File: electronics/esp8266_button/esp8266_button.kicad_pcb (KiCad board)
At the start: 2 copper layers, 34.3 x 50.8 mm, 30 parts, among them J1 CONN_01X03, J2 CONN_01X08, J3 CONN_01X08, M1 BMP180_Breakout, P1 SYMBOL, Q1 Q_NMOS_GSD, Q2 Q_PMOS_GSD, SW1 SW_Push, SW2 SW_Push, SW3 SW_Push, U1 MCP1703A-3302/MB, U2 ESP-12

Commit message: Begin next button version
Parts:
- P1: value SYMBOL -> OSHW
- R7: value R -> 320k
- R8: value R -> 100k
- U2: footprint ESP8266:ESP-12 -> ESP8266:ESP-12E
- moved U2 9.88 mm to (154.3, 94.0)
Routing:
- net GPIO0: track 31.0 -> 35.2 mm
- net GND: track 29.1 -> 31.8 mm, vias 5 -> 6
- net CH_PD: track 32.6 -> 34.7 mm
- net RESET: track 28.2 -> 30.0 mm, vias 1 -> 3
- net /GPIO5: track 16.2 -> 16.9 mm
- net /GPIO4: track 17.5 -> 18.1 mm
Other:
- board text added: "esp8266_button v1.?"
- board text added: "github.com/google/makerspace-partsbin electronics/esp8266_button"
- board text removed: "Kapton ->"
- board text removed: "esp8266_button v1"

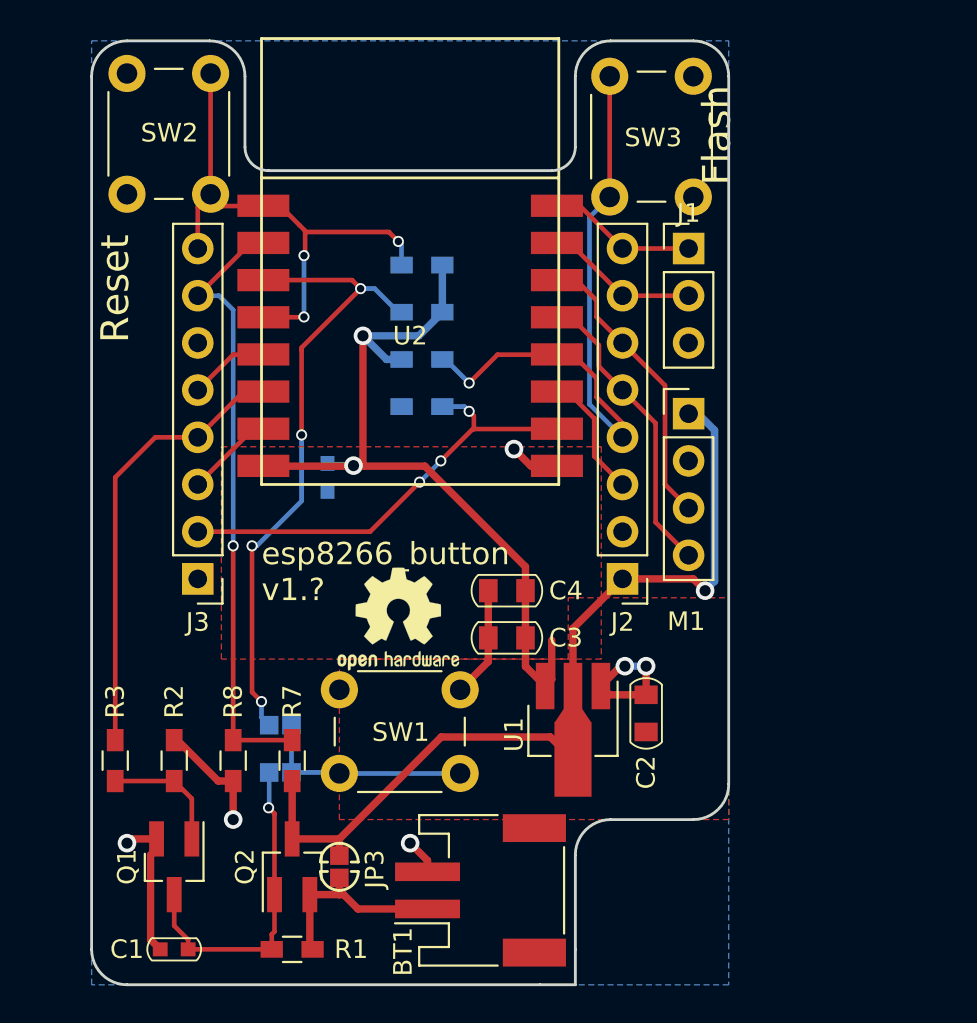
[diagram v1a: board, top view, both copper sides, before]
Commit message: esp_button almost to v1.1
Easier to solder
* Mostly 0805, with some 1206 for larger caps
* Battery connector is your choice of through hole or SMT
* Fiducials, just in case

Easier to program
* Full FTDI connector
* Auto-reset
* Pogo version below
* More obvious/accessible solder jumpers on top

Better performance
* Temperature sensor moved away from regulator :)
* Battery monitor and temperature sensor moved behind mosfet, reducing
  theoretical deep-sleep current by about 16uA

Easier to make a case for
* (Mostly) metric grid, larger board (40x50mm)
* Mounting holes (32x42mm)
* Big button slightly more centered
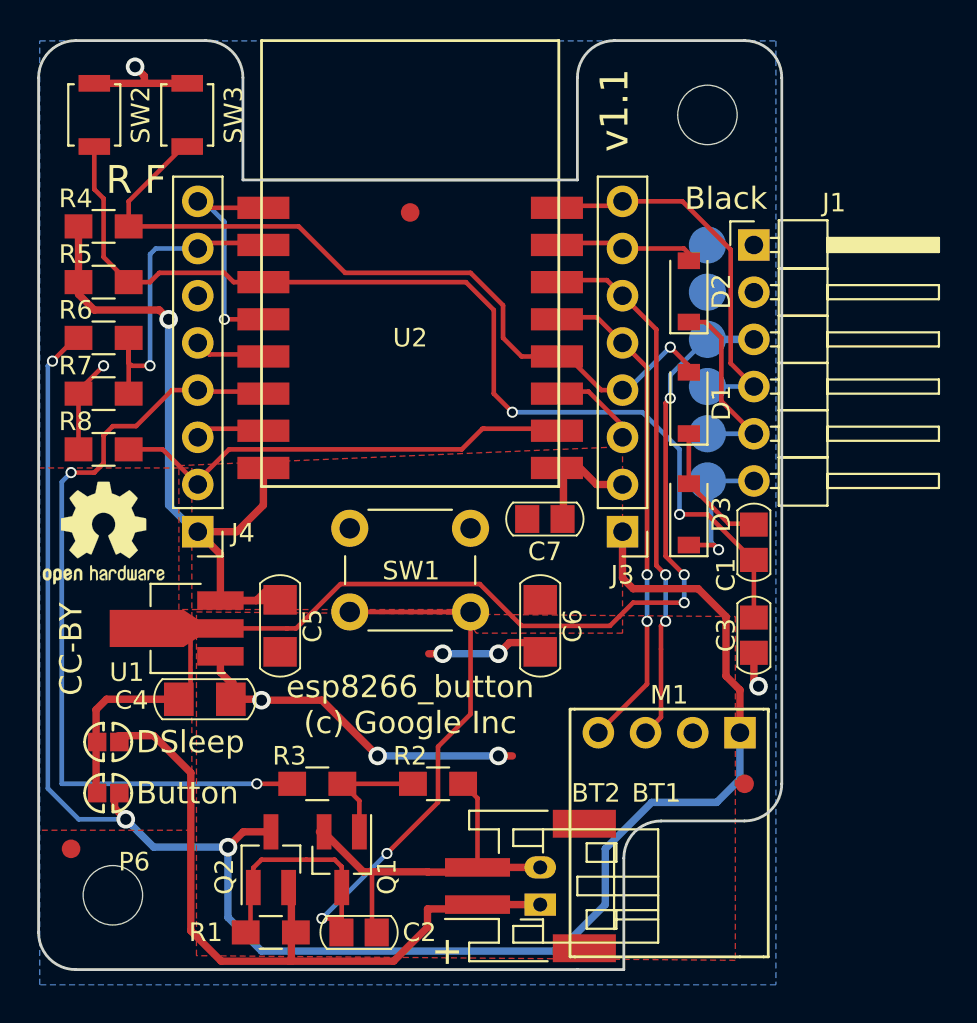
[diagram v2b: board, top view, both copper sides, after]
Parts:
- removed the JP1 at (147.3, 114.9)
- removed R9: 10k, Resistors_SMD:R_0603_HandSoldering
- added BT1: Battery_Cell, Connectors_JST:JST_PH_S2B-PH-K_02x2.00mm_Angled, F.Cu at (161.3, 124.6)
- added C6: 10u, Capacitors_SMD_Round:C_1206, F.Cu at (161.3, 109.6)
- added C7: 220p, Capacitors_SMD_Round:C_0805, F.Cu at (161.6, 103.8)
- added D1: B5819W, Diodes_SMD:D_SOD-123, F.Cu at (169.3, 97.6)
- added D2: B5819W, Diodes_SMD:D_SOD-123, F.Cu at (169.3, 91.6)
- added D3: B5819W, Diodes_SMD:D_SOD-123, F.Cu at (169.3, 103.6)
- added J2: CONN_01X06, Pogo_Pads:Pogo_6, B.Cu at (170.3, 89.1)
- added P2: M3 Hole, Mounting_Holes:MountingHole_3.2mm_M3, F.Cu at (138.3, 124.1)
- added P3: M3 Hole, Mounting_Holes:MountingHole_3.2mm_M3, F.Cu at (170.3, 82.1)
- added P4: Fid, Fiducials:Fiducial_1mm_Dia_2.54mm_Outer_CopperTop, F.Cu at (154.3, 87.3)
- added P5: Fid, Fiducials:Fiducial_1mm_Dia_2.54mm_Outer_CopperTop, F.Cu at (172.3, 118.1)
- added P6: Fid, Fiducials:Fiducial_1mm_Dia_2.54mm_Outer_CopperTop, F.Cu at (136.1, 121.6)
- C1: footprint Capacitors_SMD_Round:C_0603 -> Capacitors_SMD_Round:C_0805
- C2, C3: value 10u -> 220p
- C4: footprint Capacitors_SMD_Round:C_0805 -> Capacitors_SMD_Round:C_1206
- C5: value 0.1u -> 10u; footprint Capacitors_SMD_Round:C_0603 -> Capacitors_SMD_Round:C_1206; moved to F.Cu
- J1: value CONN_01X03 -> CONN_01X06; footprint Pin_Headers:Pin_Header_Straight_1x03_Pitch2.54mm -> Pin_Headers:Pin_Header_Angled_1x06_Pitch2.54mm
- JP2: value Button=PowerOn -> MOS Control; moved to F.Cu
- M1: footprint Pin_Headers:Pin_Header_Straight_1x04_Pitch2.54mm -> Breakout_Modules:BMxx80
- R1, R2, R3: footprint Resistors_SMD:R_0603_HandSoldering -> Resistors_SMD:R_0805_HandSoldering
- R4, R5: footprint Resistors_SMD:R_0603_HandSoldering -> Resistors_SMD:R_0805_HandSoldering; moved to F.Cu
- R6: value 10k -> 320k; footprint Resistors_SMD:R_0603_HandSoldering -> Resistors_SMD:R_0805_HandSoldering; moved to F.Cu
- R7: value 320k -> 100k; footprint Resistors_SMD:R_0603_HandSoldering -> Resistors_SMD:R_0805_HandSoldering
- R8: value 100k -> 10k; footprint Resistors_SMD:R_0603_HandSoldering -> Resistors_SMD:R_0805_HandSoldering
- SW2, SW3: footprint Buttons_Switches_THT:SW_PUSH_6mm -> Buttons_Switches_SMD:SW_SPST_B3U-1000P
- moved C1 38.1 mm to (172.8, 105.1), turned to 270 degrees
- moved SW3 27.3 mm to (142.3, 82.1)
- moved R7 22.2 mm to (137.8, 97.1), turned to 180 degrees
- moved U1 21.6 mm to (142.1, 109.7), turned to 180 degrees
- moved C2 19.4 mm to (151.6, 126.1), turned to 0 degrees
- moved R8 18.1 mm to (137.8, 100.1), turned to 0 degrees
- moved R5 17.6 mm to (137.8, 91.1), turned to 180 degrees
- moved M1 17.4 mm to (172.1, 115.3)
- moved C4 17.3 mm to (143.3, 113.5), turned to 0 degrees
- moved R4 17.3 mm to (137.8, 88.1)
- moved R6 17.2 mm to (137.8, 94.1), turned to 0 degrees
- moved P1 16.5 mm to (137.8, 104.6)
- moved R2 14.3 mm to (155.8, 118.1), turned to 0 degrees
- moved JP1 14.1 mm to (138.1, 115.8), turned to 180 degrees
- moved C3 13.3 mm to (172.8, 110.1), turned to 90 degrees
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- renumbered BT1 to BT2, J2 to J3, J3 to J4, JP3 to JP1
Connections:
- C1 pad 1: ~POWERON -> Net-(C1-Pad1)
- C1 pad 2: GND -> CH_PD
- C2 pad 1: BATTMON -> ~POWERON
- C3 pad 1: +3V3 -> GND
- C3 pad 2: GND -> CH_PD
- C4 pad 1: +3V3 -> PWRIN
- J1 pad 1: /TXD -> GND
- J1 pad 2: /RXD -> (no net)
- J1 pad 3: GND -> PWRIN
- J3 pad 7: /RXD -> RXD
- J3 pad 8: /TXD -> TXD
- J4 pad 1: (no net) -> +3V3
- J4 pad 8: RESET -> /RESET
- JP1 pad 2: BATTMON -> PWRIN
- JP2 pad 1: Net-(JP1-Pad1) -> BATTMON
- JP2 pad 2: ~POWERON -> PWRIN
- R4 pad 1: +3V3 -> GPIO0
- R4 pad 2: RESET -> +3V3
- R5 pad 1: +3V3 -> CH_PD
- R5 pad 2: GPIO0 -> +3V3
- R6 pad 1: +3V3 -> BATTMON
- R6 pad 2: CH_PD -> /ADC
- R7 pad 1: BATTMON -> /ADC
- R7 pad 2: /ADC -> GND
- R8 pad 1: /ADC -> GND
- R8 pad 2: GND -> /GPIO15
- SW1 pad 2: Net-(JP1-Pad1) -> ~POWERON
- SW2 pad 2: RESET -> CH_PD
- U1 pad 2: BATTMON -> PWRIN
- U2 pad 1: RESET -> /RESET
- U2 pad 15: /RXD -> RXD
- U2 pad 16: /TXD -> TXD
- U2 pad 4: RESET -> /RESET
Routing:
- net PWRIN: track 0.00 -> 62.3 mm, vias 0 -> 3
- net BATTMON: track 44.1 -> 96.2 mm, vias 1 -> 3
- net GND: track 31.8 -> 67.4 mm, vias 6 -> 8
- net RESET: track 30.0 -> 0.00 mm, vias 3 -> 0
- net /Vbat: track 10.6 -> 38.9 mm
- net TXD: track 0.00 -> 23.0 mm
- net ~POWERON: track 17.5 -> 39.8 mm, vias 1 -> 2
- net CH_PD: track 34.7 -> 56.1 mm, vias 4 -> 2
- net GPIO12: track 24.9 -> 44.5 mm, vias 0 -> 2
- net /ADC: track 34.3 -> 19.5 mm
- net /GPIO5: track 16.9 -> 30.9 mm, vias 0 -> 2
- net /RESET: track 0.00 -> 13.3 mm, vias 0 -> 1
- net Net-(JP1-Pad1): track 11.6 -> 0.00 mm
- net /GPIO4: track 18.1 -> 29.4 mm, vias 0 -> 2
- net Net-(D2-Pad1): track 0.00 -> 10.3 mm
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- added copper zone on F.Cu, net GND
- added copper zone on F.Cu, net PWRIN
- removed copper zone on F.Cu, net BATTMON
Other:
- board size 34.3 x 50.8 mm -> 40 x 50 mm
- board text added: "+"
- board text added: "Black"
- board text added: "Button"
- board text added: "CC-BY"
- board text added: "DSleep"
- board text added: "GND"
- board text added: "IO2"
- board text added: "R F"
- board text added: "SCL"
- board text added: "SDA"
- board text added: "esp8266_button (c) Google Inc"
- board text added: "v1.1"
- board text removed: "Flash"
- board text removed: "Reset"
- board text removed: "esp8266_button v1.?"
- board text removed: "tx rx gnd"

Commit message: Aesthetic tweaks to esp_button 1.1
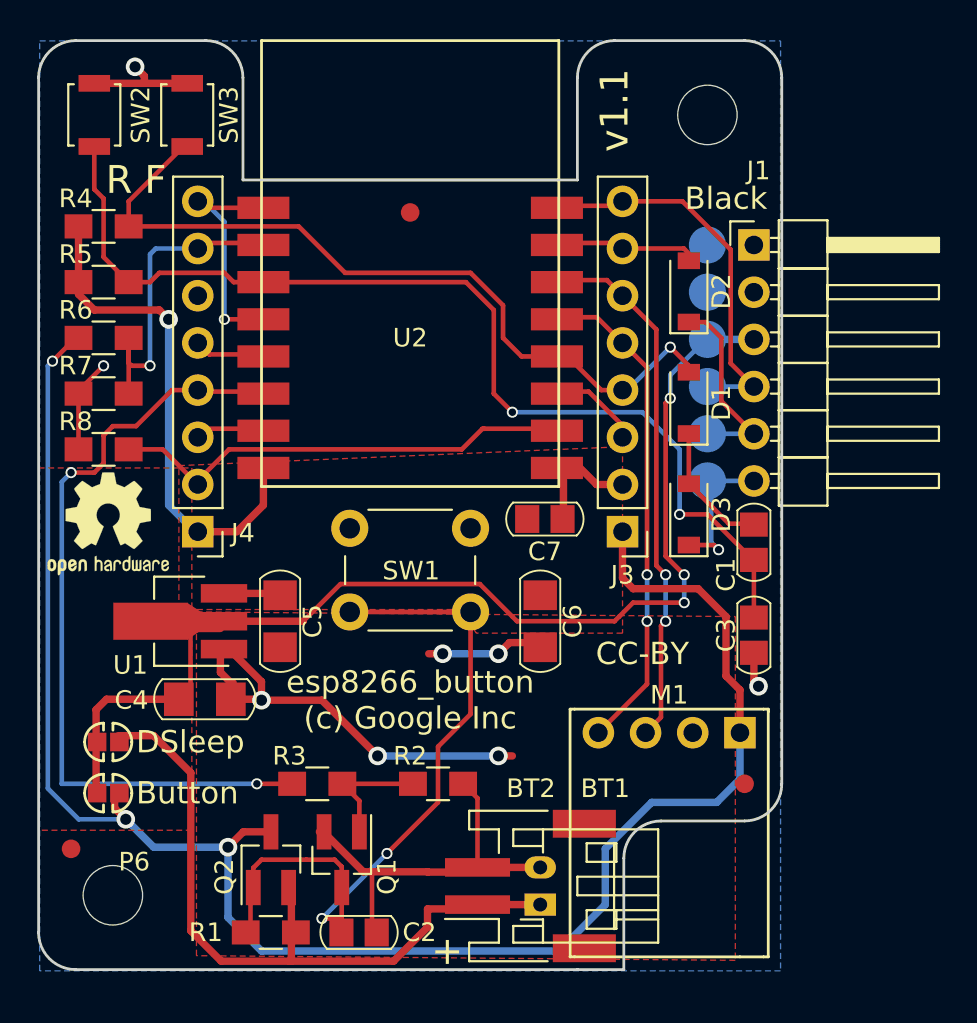
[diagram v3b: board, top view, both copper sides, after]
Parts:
- moved P1 0.56 mm to (138.1, 104.1)
- moved U1 0.43 mm to (142.3, 109.3)
- moved C5 0.25 mm to (147.3, 109.3)
- moved C6 0.25 mm to (161.3, 109.3)
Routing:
- net +3V3: track 37.6 -> 30.8 mm
- net GND: track 67.4 -> 71.1 mm
- net PWRIN: track 62.3 -> 61.8 mm
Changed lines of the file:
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@@
     (thickness 1.6)
     (drawings 38)
-    (tracks 335)
+    (tracks 334)
     (zones 0)
     (modules 40)
@@
     (descr "Through hole angled pin header, 1x06, 2.54mm pitch, 6mm pin length, single row")
     (tags "Through hole angled pin header THT 1x06 2.54mm single row")
-    (fp_text reference J1 (at 4.315 -2.27) (layer F.SilkS)
+    (fp_text reference J1 (at 0.25 -4) (layer F.SilkS)
       (effects (font (size 1 1) (thickness 0.15)))
     )
@@
     (fp_line (start 10.4 14.5) (end 10.4 -1.8) (layer F.CrtYd) (width 0.05))
     (fp_line (start 10.4 -1.8) (end -1.8 -1.8) (layer F.CrtYd) (width 0.05))
-    (fp_text user %R (at 4.315 -2.27) (layer F.Fab)
+    (fp_text user %R (at 0.25 -4) (layer F.Fab)
       (effects (font (size 1 1) (thickness 0.15)))
     )
@@
   )
   (module TO_SOT_Packages_SMD:SOT-89-3_Handsoldering (layer F.Cu)
-    (at 142.113 109.728 180)
+    (at 142.305 109.34 180)
     (descr "SOT-89-3 Handsoldering")
     (tags "SOT-89-3 Handsoldering")
@@
     (tags "connector jst ph")
     (attr smd)
-    (fp_text reference BT2 (at 5 3.5 180) (layer F.SilkS)
+    (fp_text reference BT2 (at 5.25 0 180) (layer F.SilkS)
       (effects (font (size 1 1) (thickness 0.15)))
     )
@@
   )
   (module Symbols:OSHW-Logo2_7.3x6mm_SilkScreen (layer F.Cu)
-    (at 137.805 104.59)
+    (at 138.055 104.09)
     (descr "Open Source Hardware Symbol")
     (tags "Logo Symbol OSHW")
@@
     (tags "Tactile Switch")
     (attr smd)
-    (fp_text reference SW3 (at 0 -2.5 270) (layer F.SilkS)
+    (fp_text reference SW3 (at 0 -2.25 270) (layer F.SilkS)
       (effects (font (size 1 1) (thickness 0.15)))
     )
@@
       (effects (font (size 1 1) (thickness 0.15)))
     )
-    (fp_text user %R (at 0 -2.5 270) (layer F.Fab)
+    (fp_text user %R (at 0 -2.25 270) (layer F.Fab)
       (effects (font (size 1 1) (thickness 0.15)))
     )
@@
     (descr "JST PH series connector, S2B-PH-K, side entry type, through hole, Datasheet: http://www.jst-mfg.com/product/pdf/eng/ePH.pdf")
     (tags "connector jst ph")
-    (fp_text reference BT1 (at 6 6.25 180) (layer F.SilkS)
+    (fp_text reference BT1 (at 6.25 3.5 180) (layer F.SilkS)
       (effects (font (size 1 1) (thickness 0.15)))
     )
@@
   )
   (module Capacitors_SMD_Round:C_1206 (layer F.Cu)
-    (at 161.305 109.59 270)
+    (at 161.305 109.34 270)
     (descr "Capacitor SMD 1206, reflow soldering, AVX (see smccp.pdf)")
     (tags "capacitor 1206")
@@
   )
   (module Capacitors_SMD_Round:C_1206 (layer F.Cu)
-    (at 147.305 109.59 270)
+    (at 147.305 109.34 270)
     (descr "Capacitor SMD 1206, reflow soldering, AVX (see smccp.pdf)")
     (tags "capacitor 1206")
@@
     (arrow2b (pts (xy 186.305 124.09) (xy 185.718579 122.963496)))
   )
-  (gr_text CC-BY (at 136.055 110.84 90) (layer F.SilkS)
+  (gr_text CC-BY (at 166.805 111.09) (layer F.SilkS)
     (effects (font (size 1.2 1.2) (thickness 0.3)))
   )
@@
     (effects (font (size 1 1) (thickness 0.25)) (justify left mirror))
   )
-  (gr_text "esp8266_button\n(c) Google Inc" (at 154.305 113.84) (layer F.SilkS)
+  (gr_text "esp8266_button\n(c) Google Inc" (at 154.305 113.59) (layer F.SilkS)
     (effects (font (size 1.2 1.2) (thickness 0.3)))
   )
@@
     (effects (font (size 1.5 1.5) (thickness 0.3)))
   )
+  (segment (start 144.285 110.84) (end 144.555 110.84) (width 0.4) (layer F.Cu) (net 1))
+  (segment (start 144.555 110.84) (end 146.305 112.59) (width 0.4) (layer F.Cu) (net 1))
+  (segment (start 146.305 112.59) (end 146.305 113.59) (width 0.4) (layer F.Cu) (net 1))
   (segment (start 161.305 110.49) (end 159.655 110.49) (width 0.4) (layer F.Cu) (net 1))
   (segment (start 159.655 110.49) (end 159.055 111.09) (width 0.4) (layer F.Cu) (net 1))
@@
   (segment (start 139 120) (end 140.5 121.5) (width 0.4) (layer B.Cu) (net 2))
   (via (at 139 120) (size 1) (drill 0.6) (layers F.Cu B.Cu) (net 2))
-  (segment (start 144.093 108.228) (end 147.267 108.228) (width 0.4) (layer F.Cu) (net 3))
+  (segment (start 144.285 107.84) (end 146.955 107.84) (width 0.4) (layer F.Cu) (net 3))
+  (segment (start 146.955 107.84) (end 147.305 108.19) (width 0.4) (layer F.Cu) (net 3))
   (segment (start 147.267 108.228) (end 147.305 108.19) (width 0.4) (layer F.Cu) (net 3))
-  (segment (start 144.093 108.228) (end 146.022 108.228) (width 0.4) (layer F.Cu) (net 3))
-  (segment (start 146.022 108.228) (end 146.5 107.75) (width 0.4) (layer F.Cu) (net 3))
   (segment (start 146.405 101.09) (end 146.405 103.095) (width 0.4) (layer F.Cu) (net 3))
   (segment (start 144.979 104.521) (end 142.875 104.521) (width 0.4) (layer F.Cu) (net 3))
@@
   (segment (start 136.455 88.09) (end 136.455 91.09) (width 0.4) (layer F.Cu) (net 3))
   (segment (start 142.875 104.521) (end 142.875 104.51) (width 0.4) (layer F.Cu) (net 3))
-  (segment (start 144.093 108.228) (end 144.093 105.739) (width 0.4) (layer F.Cu) (net 3))
-  (segment (start 144.093 105.739) (end 142.875 104.521) (width 0.4) (layer F.Cu) (net 3))
   (segment (start 148.305 88.09) (end 150.805 90.59) (width 0.25) (layer F.Cu) (net 4))
   (segment (start 157.555 90.59) (end 159.305 92.34) (width 0.25) (layer F.Cu) (net 4))
@@
   (segment (start 146.405 88.98) (end 143.176 88.98) (width 0.25) (layer F.Cu) (net 16))
   (segment (start 143.176 88.98) (end 142.875 89.281) (width 0.25) (layer F.Cu) (net 16))
-  (segment (start 159.805 109.09) (end 160.305 109.59) (width 0.25) (layer F.Cu) (net 17))
-  (segment (start 165.055 109.59) (end 165.555 109.09) (width 0.25) (layer F.Cu) (net 17))
-  (segment (start 160.305 109.59) (end 165.055 109.59) (width 0.25) (layer F.Cu) (net 17))
-  (segment (start 147.667 109.728) (end 148.167 109.728) (width 0.25) (layer F.Cu) (net 17))
-  (segment (start 148.167 109.728) (end 150.555 107.34) (width 0.25) (layer F.Cu) (net 17))
+  (segment (start 160.055 109.34) (end 165.305 109.34) (width 0.25) (layer F.Cu) (net 17))
+  (segment (start 144.285 109.34) (end 148.555 109.34) (width 0.4) (layer F.Cu) (net 17))
+  (segment (start 159.805 109.09) (end 160.055 109.34) (width 0.25) (layer F.Cu) (net 17))
+  (segment (start 165.305 109.34) (end 165.555 109.09) (width 0.25) (layer F.Cu) (net 17))
+  (segment (start 148.555 109.34) (end 150.555 107.34) (width 0.25) (layer F.Cu) (net 17))
   (segment (start 150.555 107.34) (end 158.055 107.34) (width 0.25) (layer F.Cu) (net 17))
   (segment (start 159.805 109.09) (end 158.055 107.34) (width 0.25) (layer F.Cu) (net 17))
@@
   (segment (start 169.055 108.34) (end 166.305 108.34) (width 0.25) (layer F.Cu) (net 17))
   (via (at 169.055 108.34) (size 0.6) (drill 0.4) (layers F.Cu B.Cu) (net 17))
-  (segment (start 147.667 109.728) (end 144.093 109.728) (width 0.25) (layer F.Cu) (net 17))
   (segment (start 170.305 94.17) (end 170.225 94.17) (width 0.25) (layer B.Cu) (net 17))
   (segment (start 142.483 109.728) (end 142.483 112.811) (width 0.25) (layer F.Cu) (net 17))
@@
     (polygon
       (pts
-        (xy 134.366 78.105) (xy 173.99 78.105) (xy 173.99 128.905) (xy 134.366 128.905)
+        (xy 134.366 78.105) (xy 174.24 78.105) (xy 174.24 128.155) (xy 134.366 128.155)
       )
     )
